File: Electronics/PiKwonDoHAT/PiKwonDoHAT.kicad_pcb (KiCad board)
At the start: 2 copper layers, 36 x 63 mm, 37 parts, among them J1 Conn_02x20_Odd_Even, J2 Judge3, J3 Judge2, J4 Judge1, J5 Controller

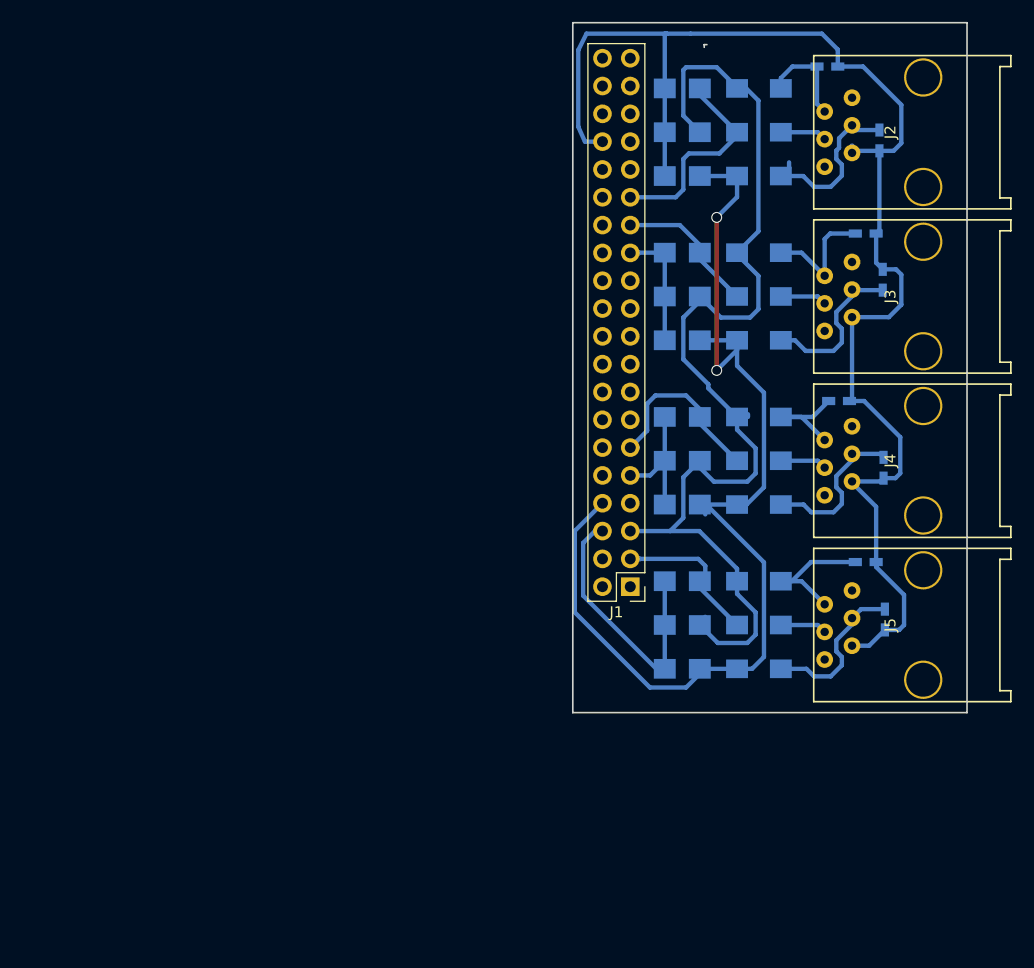
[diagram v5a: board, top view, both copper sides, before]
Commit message: Completed HAT PCB
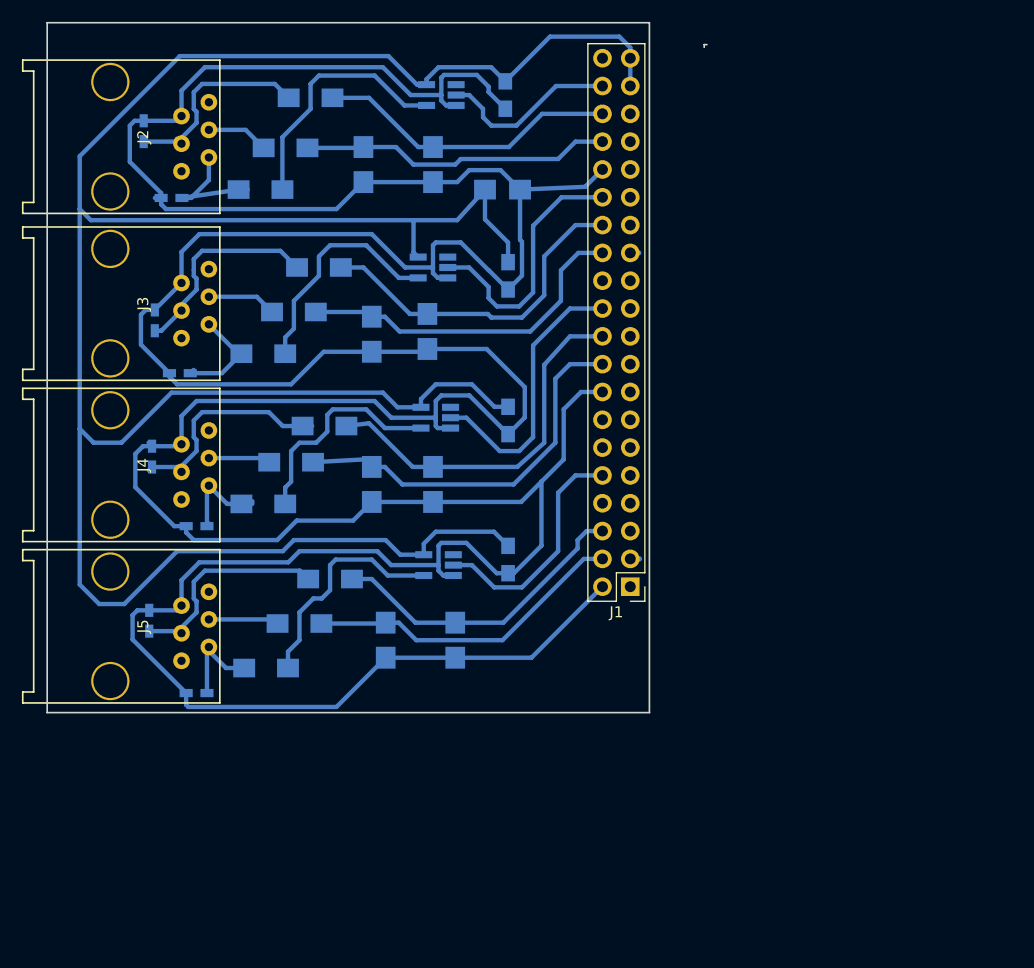
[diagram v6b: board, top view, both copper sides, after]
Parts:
- removed D2, D3, D4: D_Zener, Diodes_SMD:SOD-80C
- added C10: 10nF, Capacitors_SMD:C_0805_HandSoldering, B.Cu at (111.8, 76.6)
- added C11: 10nF, Capacitors_SMD:C_0805_HandSoldering, B.Cu at (112.1, 93.1)
- added C12: 10nF, Capacitors_SMD:C_0805_HandSoldering, B.Cu at (112.1, 119.0)
- added C9: 10nF, Capacitors_SMD:C_0805_HandSoldering, B.Cu at (112.1, 106.3)
- added U1: 74LV1T34, TO_SOT_Packages_SMD:SOT-23-5_HandSoldering, B.Cu at (106.0, 76.6)
- added U2: 74LV1T34, TO_SOT_Packages_SMD:SOT-23-5_HandSoldering, B.Cu at (105.7, 119.5)
- added U3: 74LV1T34, TO_SOT_Packages_SMD:SOT-23-5_HandSoldering, B.Cu at (105.5, 106.1)
- added U4: 74LV1T34, TO_SOT_Packages_SMD:SOT-23-5_HandSoldering, B.Cu at (105.2, 92.4)
- C1, C2, C3, C4, C5, C6, C7, C8: value 270pF -> 470pF
- D1, D10, D11, D12, D5, D6, D7, D8: value D_Zener -> D_Zener_3.3V
- D9: value D_Zener -> D_Zener_5V
- R10, R11, R12, R2, R3, R4, R5, R6, R7, R8, R9: value 470 -> 10
- moved J3 74.2 mm to (75.8, 95.7), turned to 90 degrees
- moved J2 74.2 mm to (75.8, 80.4), turned to 90 degrees
- moved J4 74.2 mm to (75.8, 110.4), turned to 90 degrees
- moved J5 74.2 mm to (75.8, 125.1), turned to 90 degrees
- moved C1 67.2 mm to (78.8, 79.9), turned to 90 degrees
- moved C4 67.2 mm to (79.3, 124.6), turned to 90 degrees
- moved C3 66.8 mm to (79.6, 109.6), turned to 90 degrees
- moved C2 66.6 mm to (79.8, 97.2)
- moved C6 63.9 mm to (82.1, 102.0), turned to 180 degrees
- moved C8 62.3 mm to (83.6, 131.2), turned to 180 degrees
- moved C5 61.1 mm to (81.4, 86.0), turned to 180 degrees
- moved C7 59.8 mm to (83.6, 116.0), turned to 180 degrees
- moved R9 46.4 mm to (89.5, 85.2), turned to 0 degrees
- moved R10 46.2 mm to (89.7, 100.2), turned to 0 degrees
- moved R11 46.0 mm to (89.7, 113.9), turned to 0 degrees
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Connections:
- D1 pad 1: Net-(D1-Pad1) -> /J1_Data
- D10 pad 1: /CLK -> /J2_Data
- D11 pad 1: /CLK -> /J3_Data
- D12 pad 1: /CLK -> /C_Data
- D5 pad 1: /LOAD -> /J1_LOAD
- D6 pad 1: /LOAD -> /J2_LOAD
- D7 pad 1: /LOAD -> /J3_LOAD
- D8 pad 1: /LOAD -> /C_LOAD
- D9 pad 1: /CLK -> +5V
- J1 pad 10: (no net) -> /CLK
- J1 pad 11: Net-(D3-Pad1) -> (no net)
- J1 pad 16: (no net) -> GND
- J1 pad 18: (no net) -> /J3_Data
- J1 pad 2: (no net) -> GND
- J1 pad 20: (no net) -> /J3_LOAD
- J1 pad 22: (no net) -> /CLK
- J1 pad 25: GND -> (no net)
- J1 pad 26: (no net) -> /J2_Data
- J1 pad 27: Net-(D2-Pad1) -> (no net)
- J1 pad 28: (no net) -> /J2_LOAD
- J1 pad 29: Net-(D1-Pad1) -> (no net)
- J1 pad 3: Net-(D4-Pad1) -> (no net)
- J1 pad 30: (no net) -> /CLK
- J1 pad 32: (no net) -> GND
- J1 pad 34: GND -> /J1_Data
- J1 pad 36: (no net) -> /J1_LOAD
- J1 pad 37: (no net) -> +5V
- J1 pad 38: (no net) -> /CLK
- J1 pad 39: (no net) -> +5V
- J1 pad 4: (no net) -> /C_Data
- J1 pad 5: /CLK -> (no net)
- J1 pad 6: GND -> /C_LOAD
- J1 pad 8: /LOAD -> (no net)
- J1 pad 9: GND -> (no net)
- R1 pad 2: Net-(D1-Pad1) -> /J1_Data
- R10 pad 2: /CLK -> Net-(R10-Pad2)
- R11 pad 2: /CLK -> Net-(R11-Pad2)
- R12 pad 2: /CLK -> Net-(R12-Pad2)
- R2 pad 2: Net-(D2-Pad1) -> /J2_Data
- R3 pad 2: Net-(D3-Pad1) -> /J3_Data
- R4 pad 2: Net-(D4-Pad1) -> /C_Data
- R5 pad 2: /LOAD -> /J1_LOAD
- R6 pad 2: /LOAD -> /J2_LOAD
- R7 pad 2: /LOAD -> /J3_LOAD
- R8 pad 2: /LOAD -> /C_LOAD
- R9 pad 2: /CLK -> Net-(R9-Pad2)
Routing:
- net +5V: track 0.00 -> 240.4 mm
- net GND: track 180.4 -> 409.1 mm
- net /LOAD: track 101.0 -> 0.00 mm, vias 2 -> 0
- net /J3_Data: track 0.00 -> 35.4 mm
- net /J3_LOAD: track 0.00 -> 34.2 mm
- net /J2_Data: track 0.00 -> 31.5 mm
- net /J2_LOAD: track 0.00 -> 31.4 mm
- net /C_Data: track 0.00 -> 29.4 mm
- net /C_LOAD: track 0.00 -> 29.3 mm
- net /J1_Data: track 0.00 -> 29.1 mm
- net /J1_LOAD: track 0.00 -> 27.8 mm
- net Net-(R9-Pad2): track 0.00 -> 23.5 mm
- net Net-(R10-Pad2): track 0.00 -> 20.9 mm
- net Net-(R12-Pad2): track 0.00 -> 20.8 mm
- net Net-(R11-Pad2): track 0.00 -> 20.1 mm
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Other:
- board size 36 x 63 mm -> 60.2 x 63 mm

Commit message: Updated HAT PCB footprints and BOM
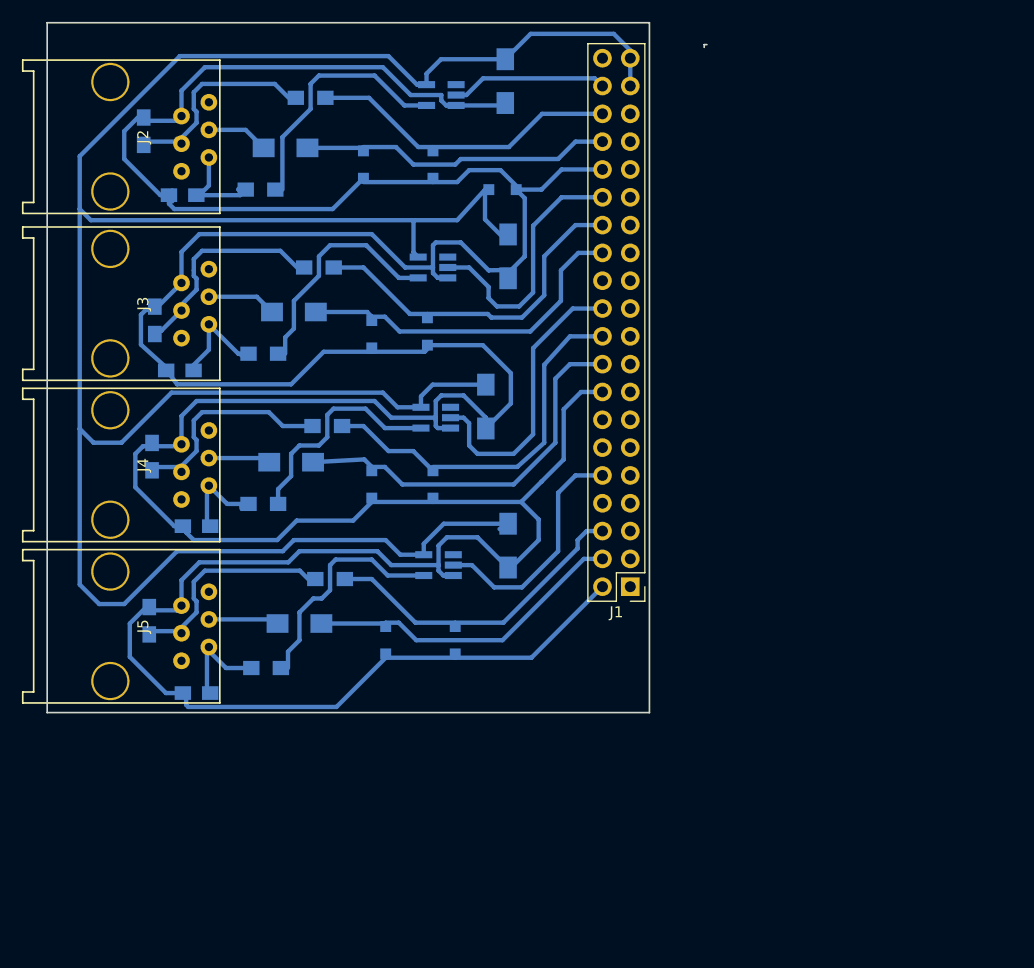
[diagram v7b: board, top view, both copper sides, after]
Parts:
- C1, C2, C3, C4, C5, C6, C7, C8: footprint Capacitors_SMD:C_0603_HandSoldering -> Capacitors_SMD:C_0805_HandSoldering
- C10, C11, C12, C9: footprint Capacitors_SMD:C_0805_HandSoldering -> Capacitors_SMD:C_1206_HandSoldering
- D1, D10, D11, D12, D5, D6, D7, D8, D9: footprint Diodes_SMD:SOD-80C -> Diodes_SMD:D_SOD-323_HandSoldering
- R10, R11, R12, R5, R6, R7, R8, R9: footprint Resistors_SMD:R_1206_HandSoldering -> Resistors_SMD:R_0805_HandSoldering
- R2, R3, R4: value 10 -> 470
- moved C9 2.40 mm to (110.1, 105.1)
- moved C11 1.78 mm to (112.1, 91.3)
- moved C12 1.27 mm to (112.1, 117.8)
- moved C10 1.27 mm to (111.8, 75.3)
- moved C5 1.05 mm to (82.4, 85.7)
- moved C6 0.25 mm to (82.1, 101.8)
- moved R7 0.25 mm to (95.6, 106.8)
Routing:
- net GND: track 409.1 -> 403.1 mm
- net +5V: track 240.4 -> 235.7 mm
- net (no net): track 3.78 -> 0.00 mm
- net /CLK: track 88.1 -> 87.0 mm
- net Net-(C5-Pad1): track 11.5 -> 10.6 mm
- net Net-(R9-Pad2): track 23.5 -> 22.8 mm
- net Net-(C3-Pad1): track 20.3 -> 19.7 mm
- net Net-(C6-Pad1): track 10.1 -> 9.46 mm

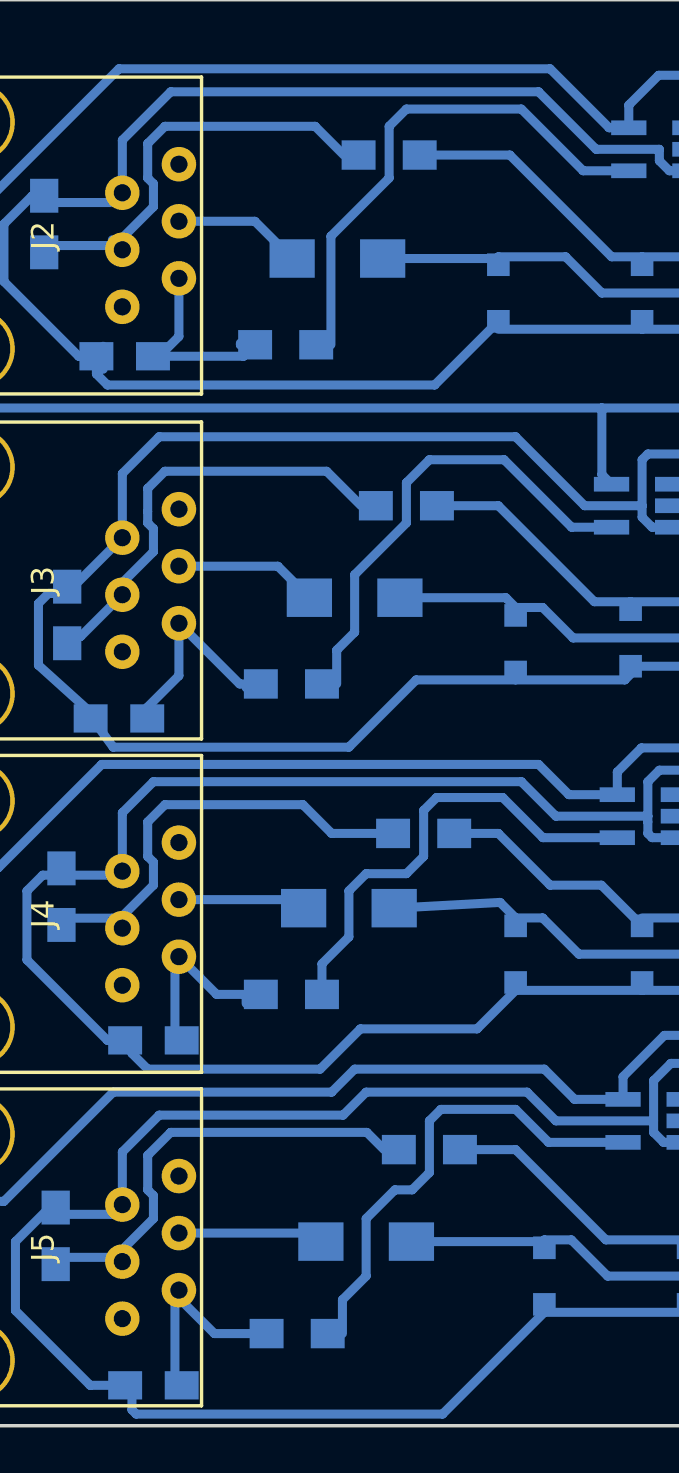
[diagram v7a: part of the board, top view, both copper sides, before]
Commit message: Updated Timer schematic, footprints, BOM, and PCB
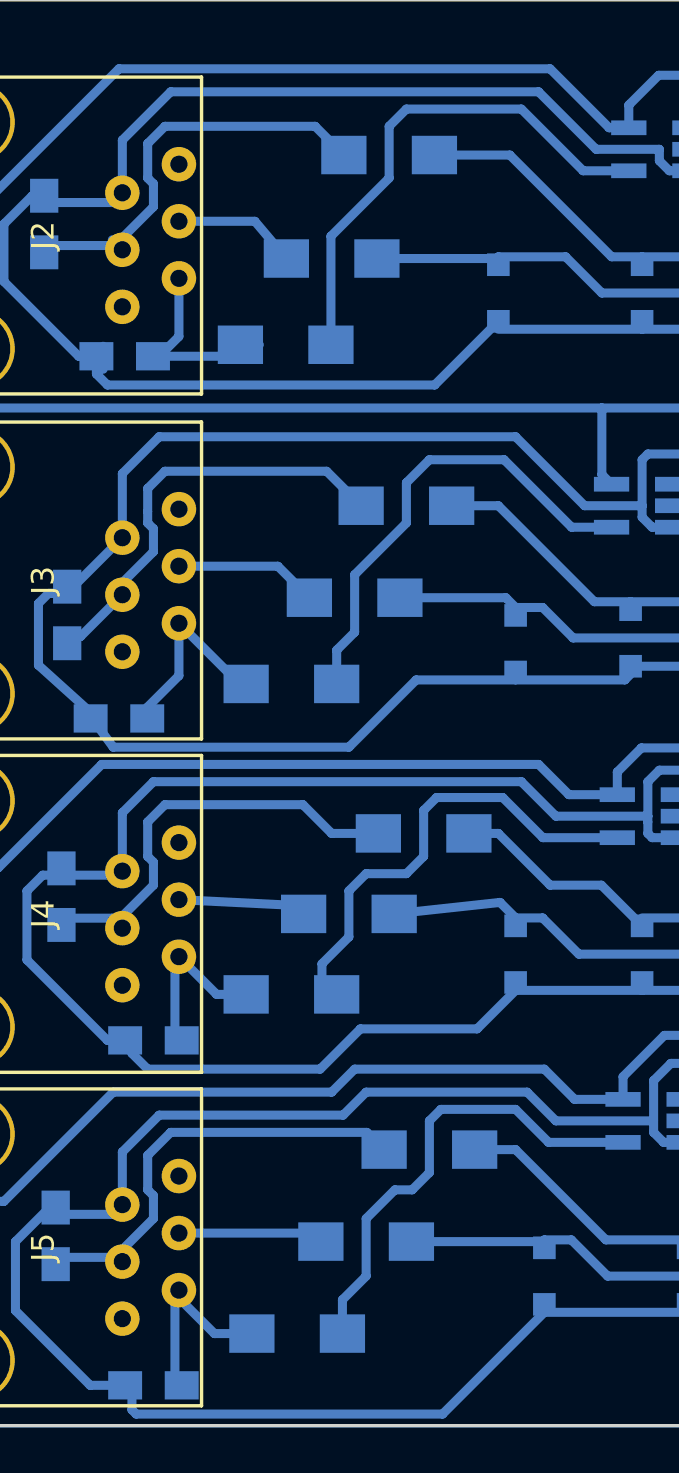
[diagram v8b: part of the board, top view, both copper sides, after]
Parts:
- R10, R11, R12, R5, R6, R7, R8, R9: footprint Resistors_SMD:R_0805_HandSoldering -> Resistors_SMD:R_1206_HandSoldering
- moved R1 0.25 mm to (91.5, 81.4)
- moved R3 0.25 mm to (92.3, 110.4)
